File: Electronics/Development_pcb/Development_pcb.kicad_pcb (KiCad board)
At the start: 2 copper layers, 14 parts, among them J1 TF-Luna, J2 Pan, J3 Tilt, J4 MP3, J5 Display, J6 LAZER, Q1 2N2222A, SW1 SW_SPST, U1 ESP32-S3-DEVKIT:C-1-N16R8, U2 MP3-TF-16P

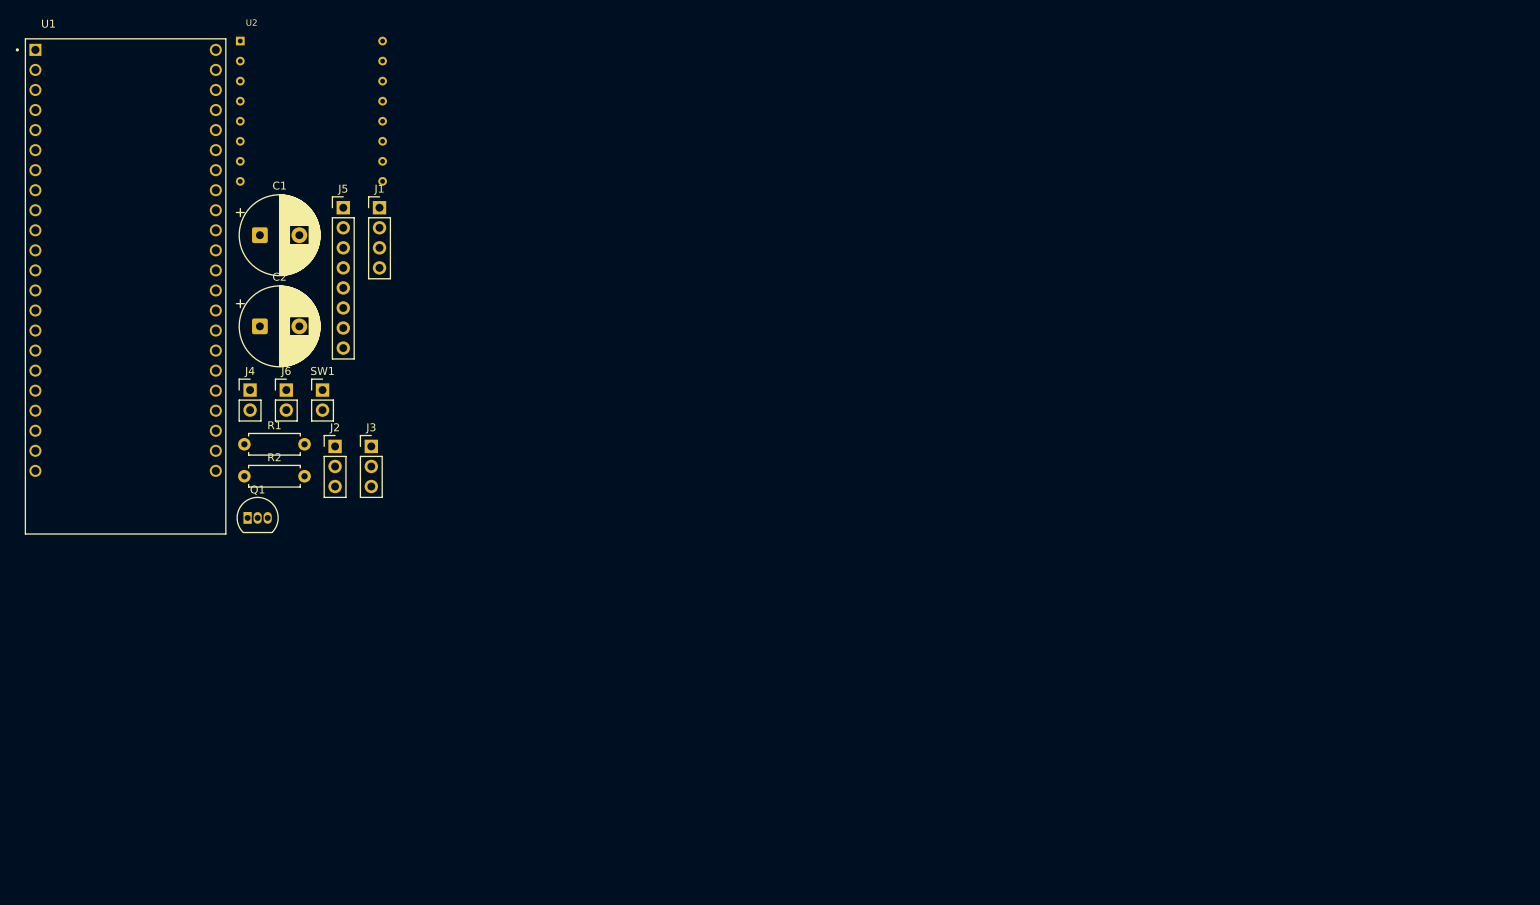
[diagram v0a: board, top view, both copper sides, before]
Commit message: Add .DS_Store files and ERC report for Development PCB
- Created .DS_Store files in Electronics and Electronics/Development_pcb directories to store custom Finder attributes.
- Added ERC report (ERC.rpt) for the Development PCB, highlighting errors related to unconnected power pins and pin type mismatches.
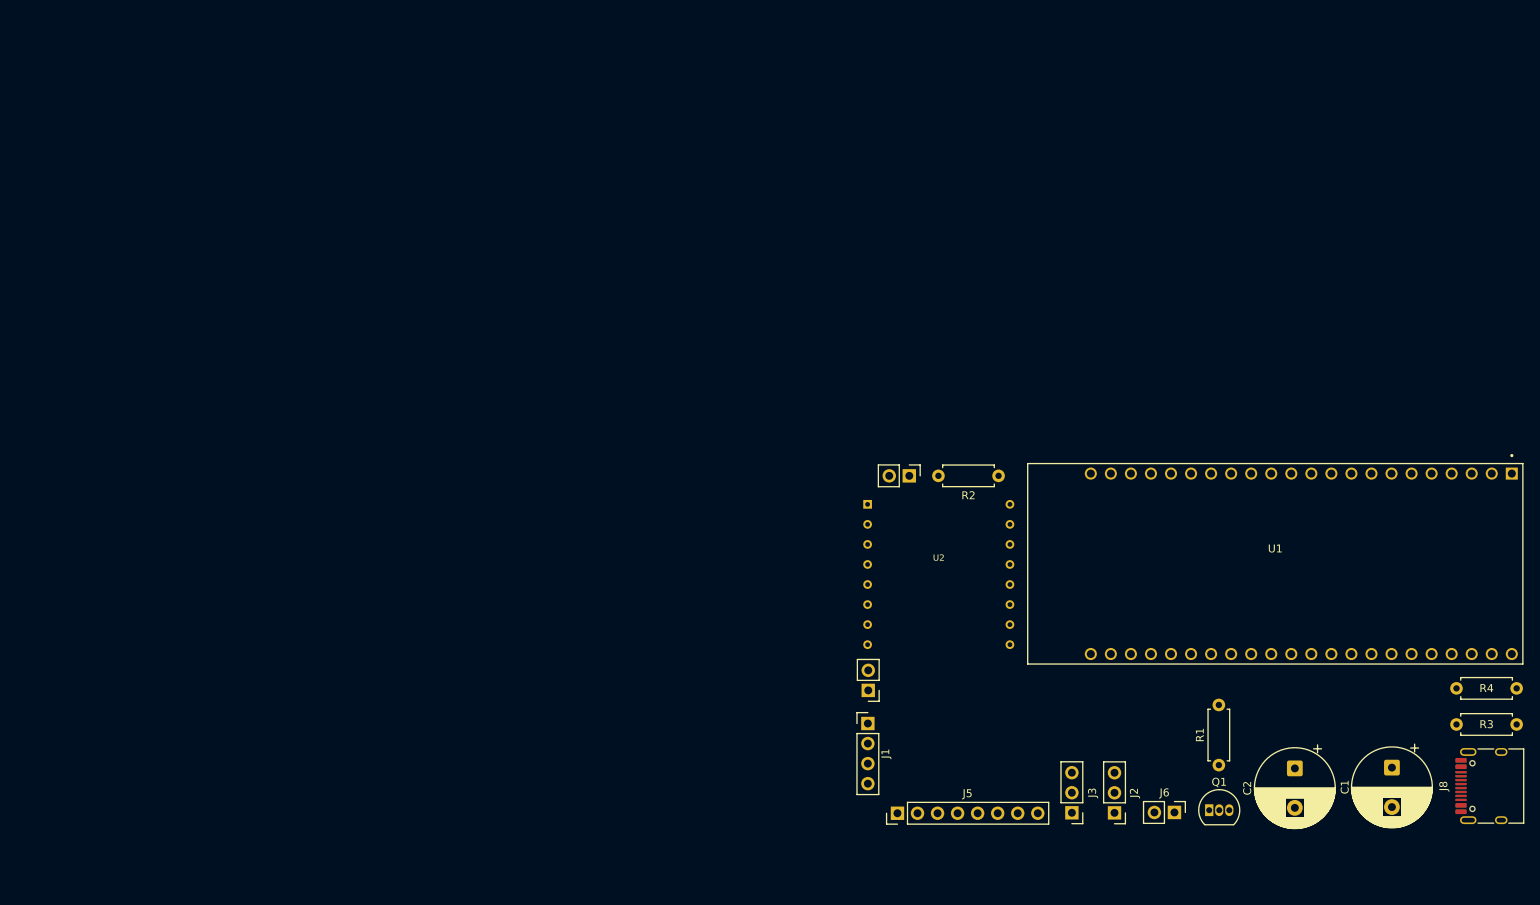
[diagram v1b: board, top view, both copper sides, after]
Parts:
- removed SW1: SW_SPST, Connector_PinHeader_2.54mm:PinHeader_1x02_P2.54mm_Vertical
- added J7: CAM-PWR, Connector_PinHeader_2.54mm:PinHeader_1x02_P2.54mm_Vertical, F.Cu at (135.2, 77.1)
- added J8: USB-C, Connector_USB:USB_C_Receptacle_HRO_TYPE-C-31-M-12, F.Cu at (209.2, 116.5)
- added R3: 5.1K, Resistor_THT:R_Axial_DIN0207_L6.3mm_D2.5mm_P7.62mm_Horizontal, F.Cu at (212.2, 108.6)
- added R4: 5.1K, Resistor_THT:R_Axial_DIN0207_L6.3mm_D2.5mm_P7.62mm_Horizontal, F.Cu at (212.2, 104.1)
- moved C1 158.5 mm to (196.4, 114.1), turned to -90 degrees
- moved U1 149.8 mm to (181.6, 88.3), turned to -90 degrees
- moved C2 142.6 mm to (184.1, 114.2), turned to -90 degrees
- moved R1 130.0 mm to (174.4, 113.8), turned to 90 degrees
- moved Q1 127.3 mm to (173.2, 119.5)
- moved J6 124.6 mm to (168.8, 119.8), turned to -90 degrees
- moved J2 109.1 mm to (161.2, 119.8), turned to 180 degrees
- moved J5 104.0 mm to (133.7, 119.9), turned to 90 degrees
- moved J3 100.2 mm to (155.8, 119.8), turned to 180 degrees
- moved U2 98.8 mm to (129.9, 80.8)
- moved J1 90.0 mm to (130.0, 108.5)
- moved R2 87.9 mm to (138.9, 77.1)
- moved J4 87.1 mm to (130.0, 104.3), turned to 180 degrees
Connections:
- J2 pad 1: Net-(J2-Pin_1) -> GND
- J2 pad 3: GND -> Net-(J2-Pin_3)
- J6 pad 2: Net-(J6-Pin_2) -> +5V
- U1 pad J1_1: unconnected-(U1-3V3-PadJ1_1) -> GND
- U1 pad J1_10: Net-(J1-Pin_2) -> unconnected-(U1-GPIO38-PadJ1_10)
- U1 pad J1_11: Net-(J1-Pin_3) -> unconnected-(U1-GPIO37-PadJ1_11)
- U1 pad J1_15: Net-(J5-Pin_4) -> unconnected-(U1-GPIO45-PadJ1_15)
- U1 pad J1_16: Net-(J5-Pin_5) -> unconnected-(U1-GPIO48-PadJ1_16)
- U1 pad J1_17: Net-(J5-Pin_6) -> unconnected-(U1-GPIO47-PadJ1_17)
- U1 pad J1_18: Net-(J5-Pin_7) -> unconnected-(U1-GPIO21-PadJ1_18)
- U1 pad J1_19: Net-(U1-GPIO13) -> unconnected-(U1-USB_D+/GPIO20-PadJ1_19)
- U1 pad J1_20: Net-(U1-GPIO14) -> unconnected-(U1-USB_D-/GPIO19-PadJ1_20)
- U1 pad J1_21: +5V -> unconnected-(U1-GND1-PadJ1_21)
- U1 pad J1_4: Net-(J2-Pin_1) -> unconnected-(U1-GPIO1-PadJ1_4)
- U1 pad J1_5: Net-(J3-Pin_3) -> unconnected-(U1-GPIO2-PadJ1_5)
- U1 pad J1_6: Net-(U1-GPIO6) -> unconnected-(U1-MTMS/GPIO42-PadJ1_6)
- U1 pad J1_8: Net-(J5-Pin_3) -> unconnected-(U1-MTDO/GPIO40-PadJ1_8)
- U1 pad J3_1: GND -> unconnected-(U1-3V3-PadJ3_1)
- U1 pad J3_10: unconnected-(U1-GPIO38-PadJ3_10) -> Net-(J1-Pin_2)
- U1 pad J3_11: unconnected-(U1-GPIO37-PadJ3_11) -> Net-(J1-Pin_3)
- U1 pad J3_15: unconnected-(U1-GPIO45-PadJ3_15) -> Net-(J5-Pin_4)
- U1 pad J3_16: unconnected-(U1-GPIO48-PadJ3_16) -> Net-(J5-Pin_5)
- U1 pad J3_17: unconnected-(U1-GPIO47-PadJ3_17) -> Net-(J5-Pin_6)
- U1 pad J3_18: unconnected-(U1-GPIO21-PadJ3_18) -> Net-(J5-Pin_7)
- U1 pad J3_19: unconnected-(U1-USB_D+/GPIO20-PadJ3_19) -> Net-(U1-GPIO13)
- U1 pad J3_20: unconnected-(U1-USB_D-/GPIO19-PadJ3_20) -> Net-(U1-GPIO14)
- U1 pad J3_21: unconnected-(U1-GND1-PadJ3_21) -> +5V
- U1 pad J3_4: unconnected-(U1-GPIO1-PadJ3_4) -> Net-(J2-Pin_3)
- U1 pad J3_5: unconnected-(U1-GPIO2-PadJ3_5) -> Net-(J3-Pin_3)
- U1 pad J3_6: unconnected-(U1-MTMS/GPIO42-PadJ3_6) -> Net-(U1-GPIO6)
- U1 pad J3_8: unconnected-(U1-MTDO/GPIO40-PadJ3_8) -> Net-(J5-Pin_3)
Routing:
- net Net-(J4-Pin_2): track 0.00 -> 0.12 mm, vias 0 -> 1

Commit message: changes
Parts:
- removed R1, R2: 1K, Resistor_THT:R_Axial_DIN0207_L6.3mm_D2.5mm_P7.62mm_Horizontal
- added C3: 470µF, Capacitor_THT:CP_Radial_D8.0mm_P3.50mm, F.Cu at (32.1, 63.5)
- added C4: 470µF, Capacitor_THT:CP_Radial_D8.0mm_P3.50mm, F.Cu at (32.1, 73.7)
- added C5: 100nF, Capacitor_THT:C_Disc_D5.0mm_W2.5mm_P5.00mm, F.Cu at (106.7, 55.9)
- added D1: SA5.0A, Diode_THT:D_DO-15_P10.16mm_Horizontal, F.Cu at (43.2, 104.1)
- added D2: 1N5819, Diode_THT:D_DO-41_SOD81_P10.16mm_Horizontal, F.Cu at (52.3, 83.8)
- added F1: Polyfuse, Capacitor_THT:C_Disc_D5.0mm_W2.5mm_P5.00mm, F.Cu at (78.7, 106.7)
- added G***: LOGO, LOGO, F.Cu at (104.1, 114.3)
- added REF**: MountingHole_3.2mm_M3, MountingHole:MountingHole_3.2mm_M3, F.Cu at (30.4, 32.9)
- added REF**: MountingHole_3.2mm_M3, MountingHole:MountingHole_3.2mm_M3, F.Cu at (30.4, 122.9)
- added REF**: MountingHole_3.2mm_M3, MountingHole:MountingHole_3.2mm_M3, F.Cu at (120.4, 32.9)
- C1: value 1000µF 16V -> 1000µF
- C2: value 1000µF 16V -> 100nF; footprint Capacitor_THT:CP_Radial_D10.0mm_P5.00mm -> Capacitor_THT:C_Disc_D5.0mm_W2.5mm_P5.00mm
- J1: value TF-Luna -> Pan-Servo; footprint Connector_PinHeader_2.54mm:PinHeader_1x04_P2.54mm_Vertical -> Connector_PinHeader_2.54mm:PinHeader_1x03_P2.54mm_Vertical
- J2: value Pan -> Tilt-Servo
- J3: value Tilt -> cam-power; footprint Connector_PinHeader_2.54mm:PinHeader_1x03_P2.54mm_Vertical -> Connector_JST:JST_XH_B2B-XH-A_1x02_P2.50mm_Vertical
- J4: value MP3 -> laser-power; footprint Connector_PinHeader_2.54mm:PinHeader_1x02_P2.54mm_Vertical -> Connector_JST:JST_XH_B2B-XH-A_1x02_P2.50mm_Vertical
- J5: value Display -> SPEAKER; footprint Connector_PinHeader_2.54mm:PinHeader_1x08_P2.54mm_Vertical -> Connector_JST:JST_XH_B2B-XH-A_1x02_P2.50mm_Vertical
- J6: value LAZER -> TFT_display; footprint Connector_PinHeader_2.54mm:PinHeader_1x02_P2.54mm_Vertical -> Connector_JST:JST_XH_B8B-XH-A_1x08_P2.50mm_Vertical
- J7: value CAM-PWR -> lidar-TOF; footprint Connector_PinHeader_2.54mm:PinHeader_1x02_P2.54mm_Vertical -> Connector_PinHeader_2.54mm:PinHeader_1x04_P2.54mm_Vertical
- J8: value USB-C -> USB_C_IN; footprint Connector_USB:USB_C_Receptacle_HRO_TYPE-C-31-M-12 -> TerminalBlock_Phoenix:TerminalBlock_Phoenix_MKDS-3-2-5.08_1x02_P5.08mm_Horizontal
- Q1: value 2N2222A -> PN2222A
- R3: value 5.1K -> 1k; footprint Resistor_THT:R_Axial_DIN0207_L6.3mm_D2.5mm_P7.62mm_Horizontal -> Resistor_THT:R_Axial_DIN0207_L6.3mm_D2.5mm_P10.16mm_Horizontal
- R4: value 5.1K -> 1kΩ; footprint Resistor_THT:R_Axial_DIN0207_L6.3mm_D2.5mm_P7.62mm_Horizontal -> Resistor_THT:R_Axial_DIN0207_L6.3mm_D2.5mm_P10.16mm_Horizontal
- U1: value ESP32-S3-DEVKIT:C-1-N16R8 -> ESP32-S3-DEVKITC-1-N8R8; footprint ESP32-S3-DEVKITC-1-N8R8:ESP32-S3-DEVKITC-1-N8R8 -> Development_pcb:ESP32-S3-DevKitC-1_Socket
- moved J6 139.4 mm to (55.8, 38.1), turned to 180 degrees
- moved J8 135.8 mm to (73.4, 119.4), turned to 0 degrees
- moved C1 135.6 mm to (61.0, 106.8)
- moved R4 134.1 mm to (92.7, 43.2), turned to 0 degrees
- moved C2 133.5 mm to (50.8, 106.8)
- moved J2 125.3 mm to (44.7, 73.7), turned to 90 degrees
- moved J3 125.2 mm to (33.8, 91.7), turned to -90 degrees
- moved R3 111.9 mm to (101.6, 91.4), turned to 90 degrees
- moved U1 107.9 mm to (88.9, 33.0), turned to 0 degrees
- moved J7 105.9 mm to (33.8, 46.8), turned to 0 degrees
- moved Q1 101.4 mm to (108.0, 41.9), turned to -90 degrees
- moved J1 96.4 mm to (44.7, 63.5), turned to 90 degrees
- moved J4 61.3 mm to (116.8, 44.5), turned to 90 degrees
- moved J5 40.1 mm to (111.8, 86.4), turned to 0 degrees
- moved U2 36.3 mm to (101.3, 58.4)
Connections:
- J1 pad 2: Net-(J1-Pin_2) -> +5V
- J1 pad 3: Net-(J1-Pin_3) -> /PAN_PWM
- J2 pad 3: Net-(J2-Pin_3) -> /TILT_PWM
- J4 pad 2: Net-(J4-Pin_2) -> +5V
- J5 pad 1: GND -> /SPK1
- J5 pad 2: +3.3V -> /SPK2
- J6 pad 1: Net-(J6-Pin_1) -> +3V3
- J6 pad 2: +5V -> /TFT_SCK
- J7 pad 1: +5V -> GND
- J7 pad 2: GND -> /LIDAR_TO_ESP
- Q1 pad 1: Net-(J6-Pin_1) -> GND
- Q1 pad 3: GND -> Net-(J4-Pin_1)
- R3 pad 1: GND -> /DF_RX
- R3 pad 2: Net-(J8-CC2) -> Net-(U2-RX)
- R4 pad 1: GND -> /LASER_CTRL
- R4 pad 2: Net-(J8-CC1) -> Net-(Q1-B)
- U1 pad J1_1: GND -> +3V3
- U1 pad J1_10: unconnected-(U1-GPIO38-PadJ1_10) -> /ESP_TO_LIDAR
- U1 pad J1_15: unconnected-(U1-GPIO45-PadJ1_15) -> /PAN_PWM
- U1 pad J1_16: unconnected-(U1-GPIO48-PadJ1_16) -> /TILT_PWM
- U1 pad J1_19: unconnected-(U1-USB_D+/GPIO20-PadJ1_19) -> /DF_RX
- U1 pad J1_20: unconnected-(U1-USB_D-/GPIO19-PadJ1_20) -> /DF_TX
- U1 pad J1_21: unconnected-(U1-GND1-PadJ1_21) -> Net-(D2-K)
- U1 pad J1_22: unconnected-(U1-GND2-PadJ1_22) -> GND
- U1 pad J1_4: unconnected-(U1-GPIO1-PadJ1_4) -> /TFT_SCK
- U1 pad J1_5: unconnected-(U1-GPIO2-PadJ1_5) -> /TFT_MOSI
- U1 pad J1_6: unconnected-(U1-MTMS/GPIO42-PadJ1_6) -> /TFT_DC
- U1 pad J1_7: unconnected-(U1-MTDI/GPIO41-PadJ1_7) -> /TFT_RST
- U1 pad J1_8: unconnected-(U1-MTDO/GPIO40-PadJ1_8) -> /TFT_CS
- U1 pad J1_9: unconnected-(U1-MTCK/GPIO39-PadJ1_9) -> /LIDAR_TO_ESP
- U1 pad J3_1: unconnected-(U1-3V3-PadJ3_1) -> GND
- U1 pad J3_10: Net-(J1-Pin_2) -> unconnected-(U1-GPIO38-PadJ3_10)
- U1 pad J3_11: Net-(J1-Pin_3) -> unconnected-(U1-GPIO37-PadJ3_11)
- U1 pad J3_15: Net-(J5-Pin_4) -> unconnected-(U1-GPIO45-PadJ3_15)
- U1 pad J3_16: Net-(J5-Pin_5) -> unconnected-(U1-GPIO48-PadJ3_16)
- U1 pad J3_17: Net-(J5-Pin_6) -> unconnected-(U1-GPIO47-PadJ3_17)
- U1 pad J3_18: Net-(J5-Pin_7) -> unconnected-(U1-GPIO21-PadJ3_18)
- U1 pad J3_19: Net-(U1-GPIO13) -> unconnected-(U1-USB_D+/GPIO20-PadJ3_19)
- U1 pad J3_20: Net-(U1-GPIO14) -> unconnected-(U1-USB_D-/GPIO19-PadJ3_20)
- U1 pad J3_21: +5V -> GND
- U1 pad J3_22: unconnected-(U1-GND3-PadJ3_22) -> GND
- U1 pad J3_4: Net-(J2-Pin_3) -> unconnected-(U1-GPIO1-PadJ3_4)
- U1 pad J3_5: Net-(J3-Pin_3) -> /LASER_CTRL
- U1 pad J3_6: Net-(U1-GPIO6) -> unconnected-(U1-MTMS/GPIO42-PadJ3_6)
- U1 pad J3_8: Net-(J5-Pin_3) -> unconnected-(U1-MTDO/GPIO40-PadJ3_8)
- U2 pad P$3: Net-(U1-GPIO13) -> /DF_TX
- U2 pad P$6: Net-(J4-Pin_1) -> /SPK2
- U2 pad P$7: unconnected-(U2-GND-PadP$7) -> GND
- U2 pad P$8: Net-(J4-Pin_2) -> /SPK1
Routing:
- net +5V: track 0.00 -> 290.1 mm
- net /DF_TX: track 0.00 -> 104.3 mm, vias 0 -> 1
- net /DF_RX: track 0.00 -> 45.5 mm, vias 0 -> 1
- net +3V3: track 0.00 -> 36.1 mm
- net /TFT_CS: track 0.00 -> 31.5 mm
- net /LIDAR_TO_ESP: track 0.00 -> 31.4 mm
- net /ESP_TO_LIDAR: track 0.00 -> 31.4 mm
- net /TFT_RST: track 0.00 -> 26.4 mm
- net /SPK2: track 0.00 -> 23.7 mm
- net Net-(U2-RX): track 0.00 -> 22.6 mm
- net /TFT_DC: track 0.00 -> 21.3 mm
- net /SPK1: track 0.00 -> 17.6 mm
- net /PAN_PWM: track 0.00 -> 16.7 mm
- net /TFT_MOSI: track 0.00 -> 16.3 mm
- net /TILT_PWM: track 0.00 -> 14.8 mm
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- added copper zone on B.Cu, net GND
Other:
- board outline added: 100 x 100 mm
